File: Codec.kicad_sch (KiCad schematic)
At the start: 58 parts, among them IC401 PCM3060PWR, J202 Screw_Terminal_01x02, U401 TLV9161IDBVR, U402 TLV9161IDBVR, U403 TLV9161IDBVR, U406 TLV9161IDBVR, U407 TLV9161IDBVR

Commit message: Refactoring
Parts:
- C206: JLCPCB Part # (none) -> C77081
- C401, C409, C419, C423: JLCPCB Part # (none) -> C106205
- C402, C403, C404, C420, C421: JLCPCB Part # (none) -> C432917
- C405: JLCPCB Part # (none) -> C129303
- C406: JLCPCB Part # (none) -> C386111
- C407, C422: JLCPCB Part # (none) -> C77045
- C408, C410, C424: JLCPCB Part # (none) -> C126577
- C428, C430, C432: JLCPCB Part # (none) -> C380314
- C429, C431, C433: value 0.1u -> 100n; JLCPCB Part # (none) -> C432917
- D203: JLCPCB Part # (none) -> C908769; JLCPCB Part# C908769 -> (none)
- IC401: JLCPCB Part # (none) -> C2651841; JLCPCB Part# C2651841 -> (none)
- J202: JLCPCB Part # (none) -> C3029316; JLCPCB Part# C3029316 -> (none)
- R302: JLCPCB Part # (none) -> C103557
- R401, R403, R404: JLCPCB Part # (none) -> C102758
- R402, R409: JLCPCB Part # (none) -> C409676
- R405, R421: JLCPCB Part # (none) -> C103830
- R406, R422: JLCPCB Part # (none) -> C116691
- R407, R423: JLCPCB Part # (none) -> C136588
- R408, R425: JLCPCB Part # (none) -> C279985
- R410: JLCPCB Part # (none) -> C192169
- R411: JLCPCB Part # (none) -> C318133
- R417, R418: JLCPCB Part # (none) -> C103210
- R427, R429: JLCPCB Part # (none) -> C176114
- U401, U402, U403, U406, U407: JLCPCB Part # (none) -> C4368955; JLCPCB Part# C4368955 -> (none)

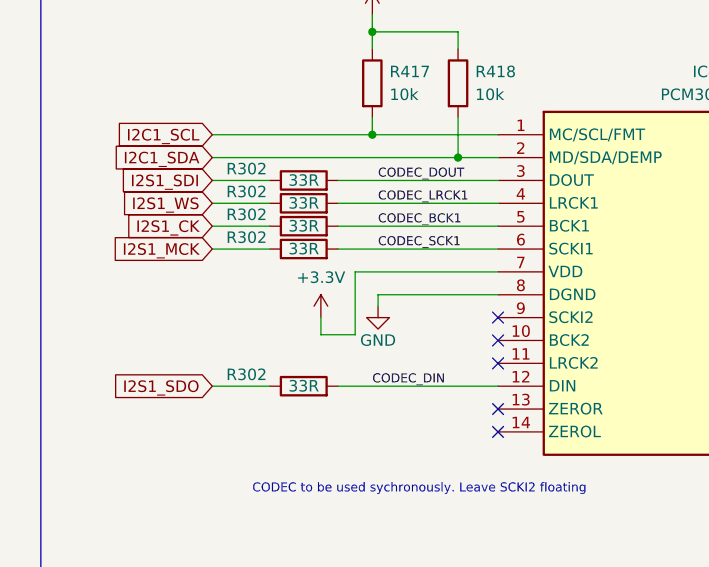
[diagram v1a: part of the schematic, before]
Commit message: Updated 33R resistors to 0R and changed MCU to H723 from H733
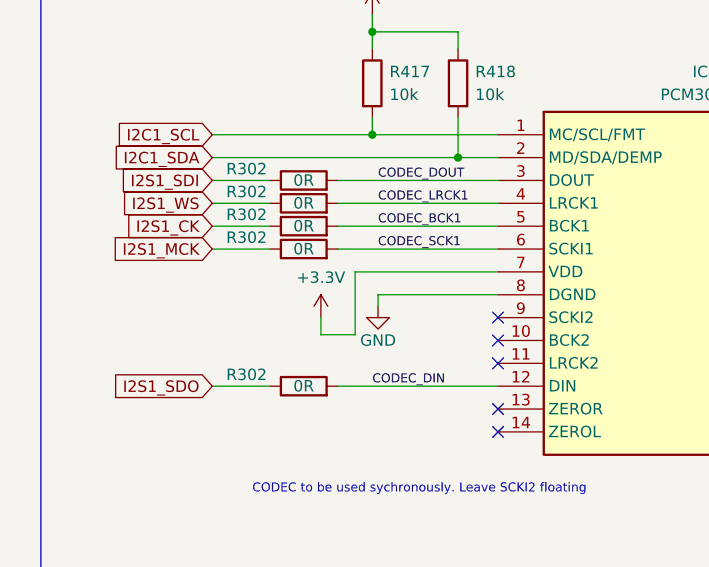
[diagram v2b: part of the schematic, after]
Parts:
- R302: value 33R -> 0R; JLCPCB Part # C103557 -> (none)
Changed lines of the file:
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@@
       (effects (font (size 1.27 1.27)))
     )
-    (property "Value" "33R" (at 47.625 196.85 90)
+    (property "Value" "0R" (at 47.625 196.85 90)
       (effects (font (size 1.27 1.27)))
     )
@@
       (effects (font (size 1.27 1.27)) hide)
     )
-    (property "JLCPCB Part #" "C103557" (at 47.625 196.85 0)
+    (property "JLCPCB Part #" "" (at 47.625 196.85 0)
       (effects (font (size 1.27 1.27)) hide)
     )
@@
       (effects (font (size 1.27 1.27)))
     )
-    (property "Value" "33R" (at 47.625 201.93 90)
+    (property "Value" "0R" (at 47.625 201.93 90)
       (effects (font (size 1.27 1.27)))
     )
@@
       (effects (font (size 1.27 1.27)) hide)
     )
-    (property "JLCPCB Part #" "C103557" (at 47.625 201.93 0)
+    (property "JLCPCB Part #" "" (at 47.625 201.93 0)
       (effects (font (size 1.27 1.27)) hide)
     )
@@
       (effects (font (size 1.27 1.27)))
     )
-    (property "Value" "33R" (at 47.625 219.71 90)
+    (property "Value" "0R" (at 47.625 219.71 90)
       (effects (font (size 1.27 1.27)))
     )
@@
       (effects (font (size 1.27 1.27)) hide)
     )
-    (property "JLCPCB Part #" "C103557" (at 47.625 219.71 0)
+    (property "JLCPCB Part #" "" (at 47.625 219.71 0)
       (effects (font (size 1.27 1.27)) hide)
     )
@@
       (effects (font (size 1.27 1.27)))
     )
-    (property "Value" "33R" (at 47.625 204.47 90)
+    (property "Value" "0R" (at 47.625 204.47 90)
       (effects (font (size 1.27 1.27)))
     )
@@
       (effects (font (size 1.27 1.27)) hide)
     )
-    (property "JLCPCB Part #" "C103557" (at 47.625 204.47 0)
+    (property "JLCPCB Part #" "" (at 47.625 204.47 0)
       (effects (font (size 1.27 1.27)) hide)
     )
@@
       (effects (font (size 1.27 1.27)))
     )
-    (property "Value" "33R" (at 47.625 199.39 90)
+    (property "Value" "0R" (at 47.625 199.39 90)
       (effects (font (size 1.27 1.27)))
     )
@@
       (effects (font (size 1.27 1.27)) hide)
     )
-    (property "JLCPCB Part #" "C103557" (at 47.625 199.39 0)
-      (effects (font (size 1.27 1.27)) hide)
-    )
+    (property "JLCPCB Part #" "" (at 47.625 199.39 0)
+      (effects (font (size 1.27 1.27)) hide)
+    )

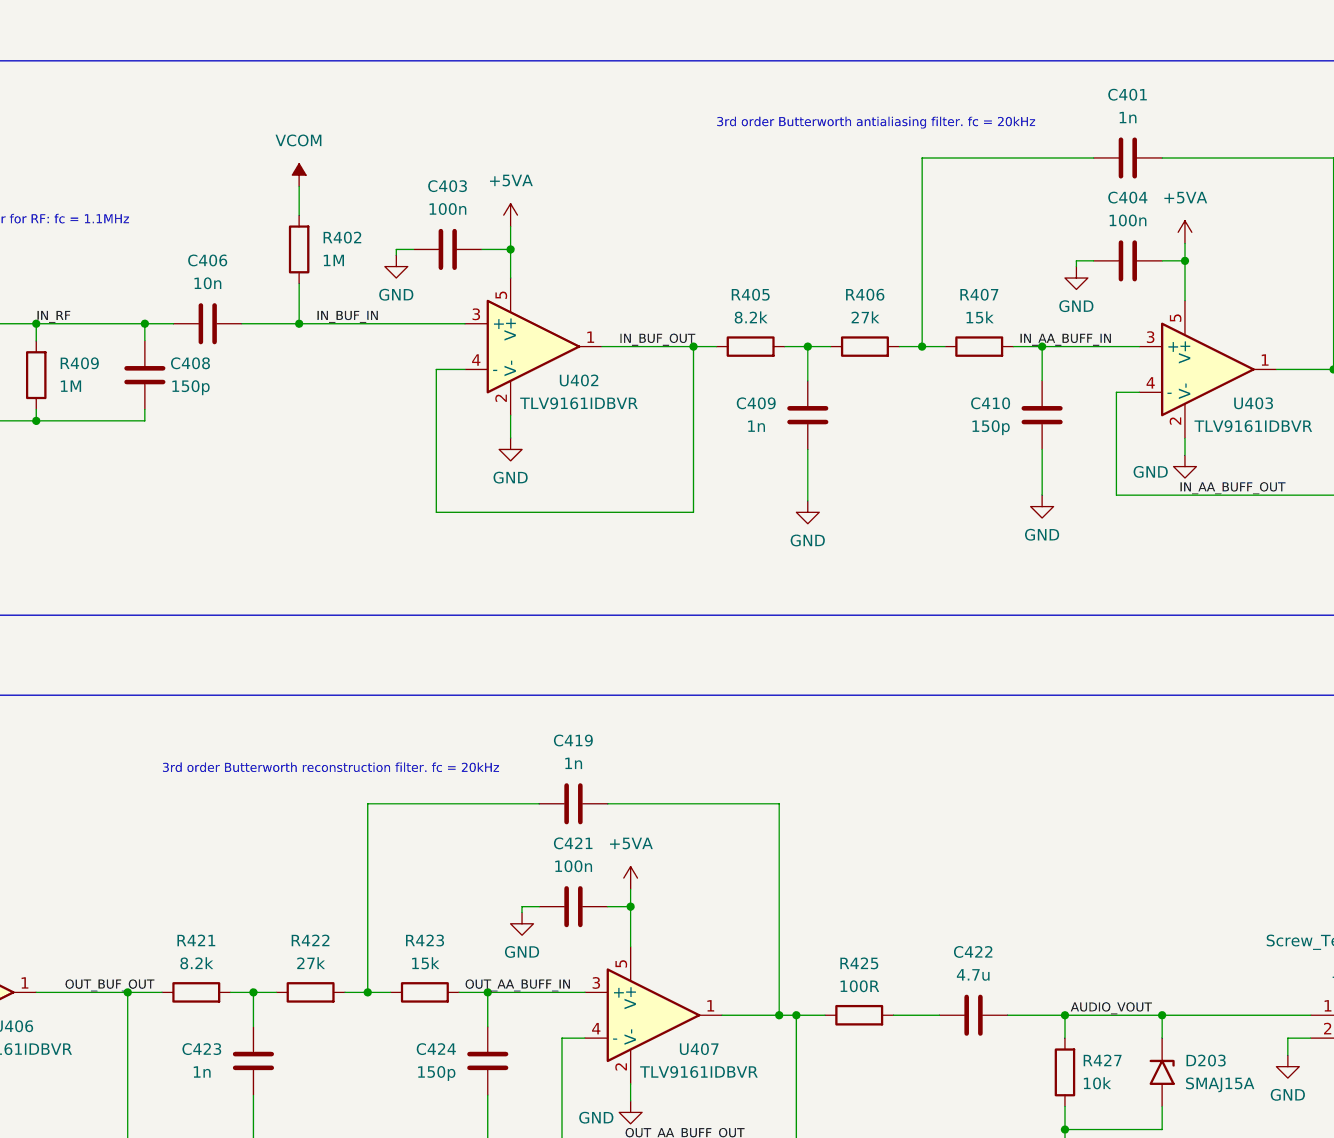
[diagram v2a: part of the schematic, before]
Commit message: Updated butterworth fc to 25khz, and changed jlc part numbers for resitors and caps
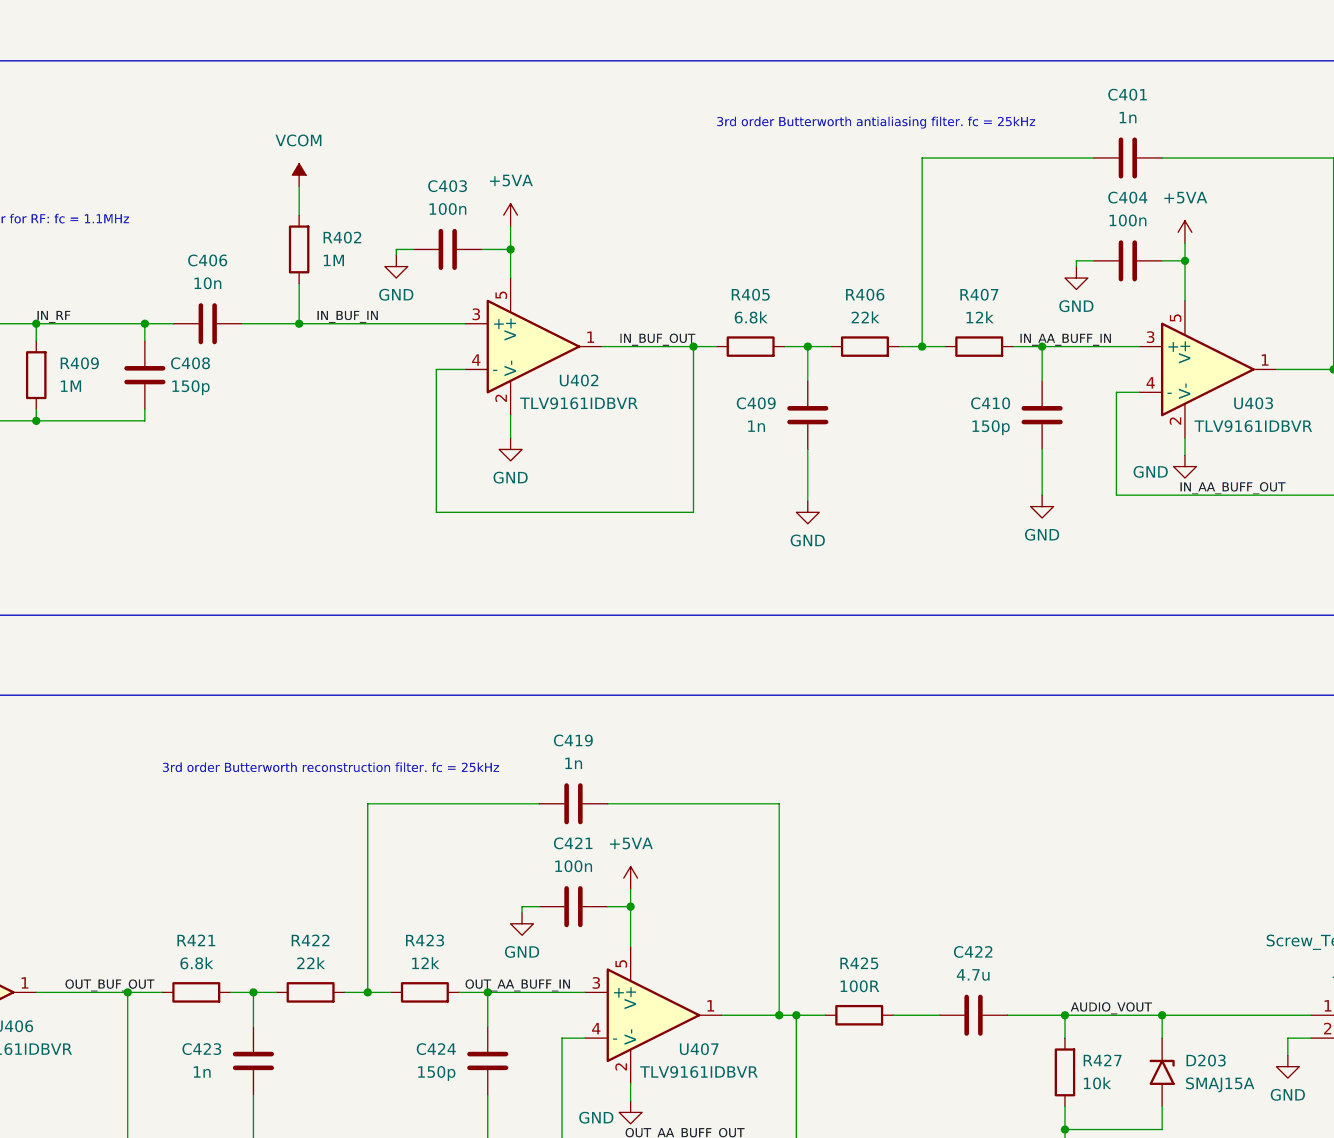
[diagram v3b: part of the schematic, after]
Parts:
- R302: JLCPCB Part # (none) -> C304185
- R405, R421: value 8.2k -> 6.8k; JLCPCB Part # C103830 -> C318134
- R406, R422: value 27k -> 22k; JLCPCB Part # C116691 -> C285211
- R407, R423: value 15k -> 12k; JLCPCB Part # C136588 -> C318136
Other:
- note added: "3rd order Butterworth antialiasing filter. fc = 25kHz"
- note added: "3rd order Butterworth reconstruction filter. fc = 25kHz"
- note removed: "3rd order Butterworth antialiasing filter. fc = 20kHz"
- note removed: "3rd order Butterworth reconstruction filter. fc = 20kHz"
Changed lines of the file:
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@@
     (effects (font (size 1 1)) (justify left bottom))
   )
-  (text "3rd order Butterworth reconstruction filter. fc = 20kHz "
+  (text "3rd order Butterworth reconstruction filter. fc = 25kHz "
     (at 81.915 99.06 0)
     (effects (font (size 1 1)) (justify left bottom))
@@
     (effects (font (size 1 1)) (justify left bottom))
   )
-  (text "3rd order Butterworth antialiasing filter. fc = 20kHz "
+  (text "3rd order Butterworth antialiasing filter. fc = 25kHz "
     (at 143.51 27.305 0)
     (effects (font (size 1 1)) (justify left bottom))
@@
       (effects (font (size 1.27 1.27)))
     )
-    (property "Value" "15k" (at 172.72 48.26 90)
+    (property "Value" "12k" (at 172.72 48.26 90)
       (effects (font (size 1.27 1.27)))
     )
@@
       (effects (font (size 1.27 1.27)) hide)
     )
-    (property "JLCPCB Part #" "C136588" (at 172.72 51.435 0)
+    (property "JLCPCB Part #" "C318136" (at 172.72 51.435 0)
       (effects (font (size 1.27 1.27)) hide)
     )
@@
       (effects (font (size 1.27 1.27)) hide)
     )
-    (property "JLCPCB Part #" "" (at 47.625 196.85 0)
+    (property "JLCPCB Part #" "C304185" (at 47.625 196.85 0)
       (effects (font (size 1.27 1.27)) hide)
     )
@@
       (effects (font (size 1.27 1.27)) hide)
     )
-    (property "JLCPCB Part #" "" (at 47.625 201.93 0)
+    (property "JLCPCB Part #" "C304185" (at 47.625 201.93 0)
       (effects (font (size 1.27 1.27)) hide)
     )
@@
       (effects (font (size 1.27 1.27)))
     )
-    (property "Value" "27k" (at 160.02 48.26 90)
+    (property "Value" "22k" (at 160.02 48.26 90)
       (effects (font (size 1.27 1.27)))
     )
@@
       (effects (font (size 1.27 1.27)) hide)
     )
-    (property "JLCPCB Part #" "C116691" (at 160.02 51.435 0)
+    (property "JLCPCB Part #" "C285211" (at 160.02 51.435 0)
       (effects (font (size 1.27 1.27)) hide)
     )
@@
       (effects (font (size 1.27 1.27)))
     )
-    (property "Value" "8.2k" (at 147.32 48.26 90)
+    (property "Value" "6.8k" (at 147.32 48.26 90)
       (effects (font (size 1.27 1.27)))
     )
@@
       (effects (font (size 1.27 1.27)) hide)
     )
-    (property "JLCPCB Part #" "C103830" (at 147.32 51.435 0)
+    (property "JLCPCB Part #" "C318134" (at 147.32 51.435 0)
       (effects (font (size 1.27 1.27)) hide)
     )
@@
       (effects (font (size 1.27 1.27)) hide)
     )
-    (property "JLCPCB Part #" "" (at 47.625 219.71 0)
+    (property "JLCPCB Part #" "C304185" (at 47.625 219.71 0)
       (effects (font (size 1.27 1.27)) hide)
     )
@@
       (effects (font (size 1.27 1.27)))
     )
-    (property "Value" "8.2k" (at 85.725 120.015 90)
+    (property "Value" "6.8k" (at 85.725 120.015 90)
       (effects (font (size 1.27 1.27)))
     )
@@
       (effects (font (size 1.27 1.27)) hide)
     )
-    (property "JLCPCB Part #" "C103830" (at 85.725 123.19 0)
+    (property "JLCPCB Part #" "C318134" (at 85.725 123.19 0)
       (effects (font (size 1.27 1.27)) hide)
     )
@@
       (effects (font (size 1.27 1.27)))
     )
-    (property "Value" "27k" (at 98.425 120.015 90)
+    (property "Value" "22k" (at 98.425 120.015 90)
       (effects (font (size 1.27 1.27)))
     )
@@
       (effects (font (size 1.27 1.27)) hide)
     )
-    (property "JLCPCB Part #" "C116691" (at 98.425 123.19 0)
+    (property "JLCPCB Part #" "C285211" (at 98.425 123.19 0)
       (effects (font (size 1.27 1.27)) hide)
     )
@@
       (effects (font (size 1.27 1.27)) hide)
     )
-    (property "JLCPCB Part #" "" (at 47.625 204.47 0)
+    (property "JLCPCB Part #" "C304185" (at 47.625 204.47 0)
       (effects (font (size 1.27 1.27)) hide)
     )
@@
       (effects (font (size 1.27 1.27)) hide)
     )
-    (property "JLCPCB Part #" "" (at 47.625 199.39 0)
+    (property "JLCPCB Part #" "C304185" (at 47.625 199.39 0)
       (effects (font (size 1.27 1.27)) hide)
     )
@@
       (effects (font (size 1.27 1.27)))
     )
-    (property "Value" "15k" (at 111.125 120.015 90)
+    (property "Value" "12k" (at 111.125 120.015 90)
       (effects (font (size 1.27 1.27)))
     )
@@
       (effects (font (size 1.27 1.27)) hide)
     )
-    (property "JLCPCB Part #" "C136588" (at 111.125 123.19 0)
-      (effects (font (size 1.27 1.27)) hide)
-    )
+    (property "JLCPCB Part #" "C318136" (at 111.125 123.19 0)
+      (effects (font (size 1.27 1.27)) hide)
+    )
